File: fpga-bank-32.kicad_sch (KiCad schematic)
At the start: 1 part, among them U1 XC7K410T-2FFG900I

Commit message: Updated schematic page fields
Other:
- company: (none) -> Antmicro Ltd.
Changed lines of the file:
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@@
   (title_block
     (title "K410T devboard")
-    (date "2023-01-04")
+    (date "2023-01-27")
     (rev "0.0.99")
+    (company "Antmicro Ltd.")
   )
   (no_connect (at 143.51 124.46))

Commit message: Adding JTAG to FMC connector - in progress
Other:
- company: Antmicro Ltd. -> (none)
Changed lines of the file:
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@@
   (title_block
     (title "K410T devboard")
-    (date "2023-01-27")
+    (date "2023-01-04")
     (rev "0.0.99")
-    (company "Antmicro Ltd.")
   )
   (no_connect (at 143.51 124.46))

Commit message: Bump revision to 1.0.0. Update name on schematic and PCB sheets
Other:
- title: K410T devboard -> Kintex 410T devboard

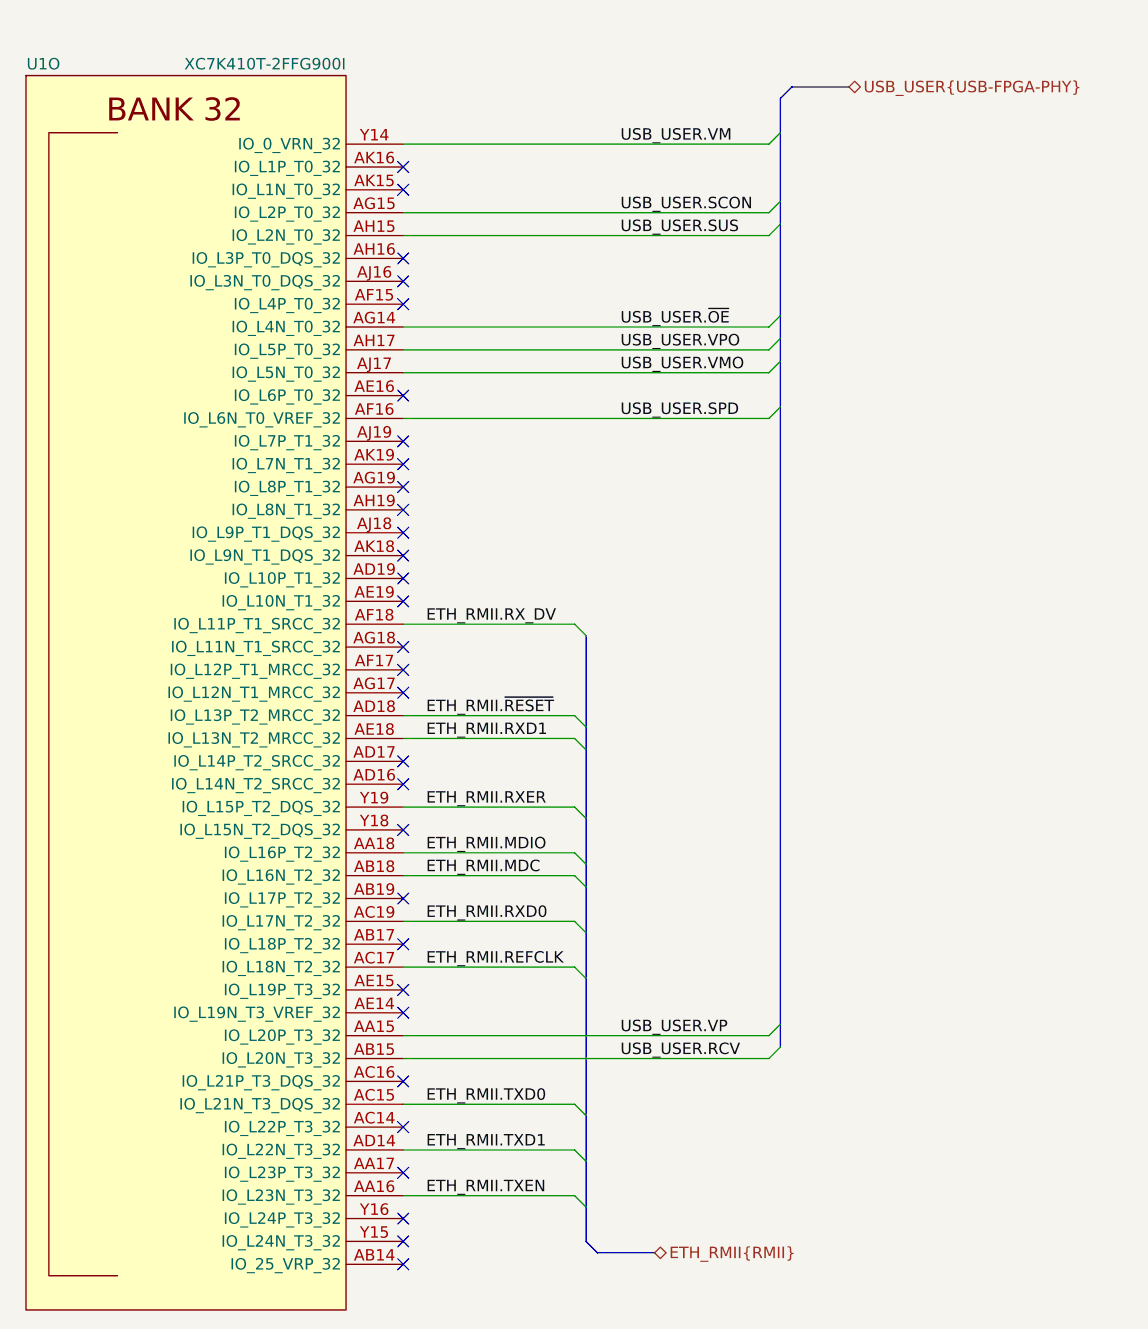
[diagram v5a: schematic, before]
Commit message: Introduce component standardization
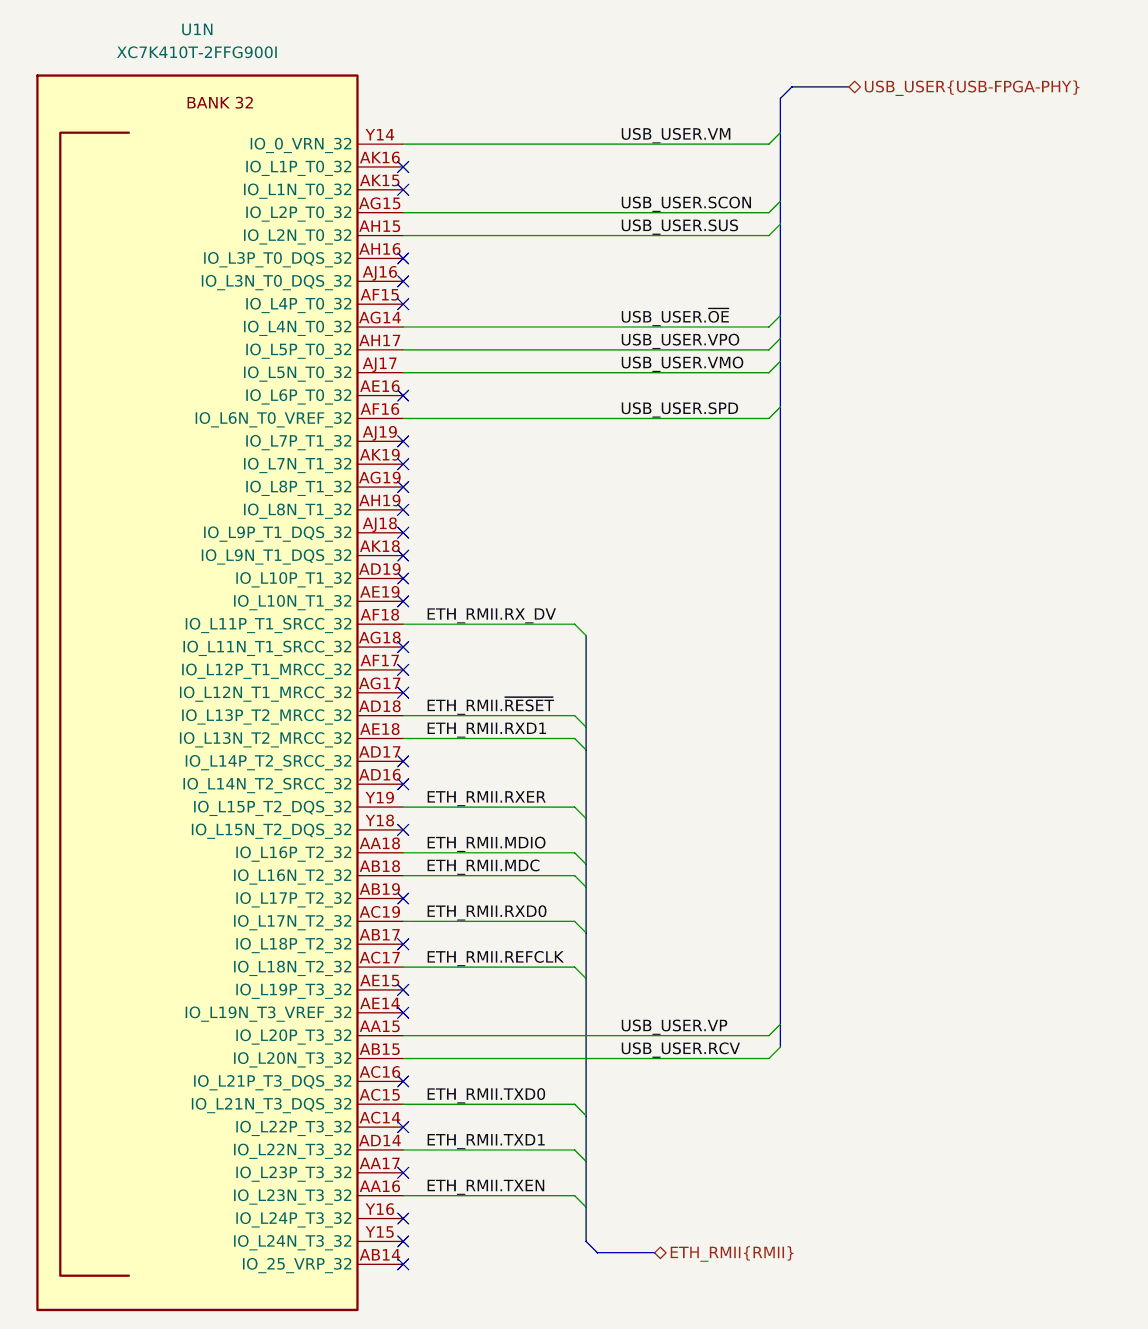
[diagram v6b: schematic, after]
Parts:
- removed U1: XC7K410T-2FFG900I, K410T-devboard-footprints:xc7k410t-2ffg900I, symbol K410T-devboard:XC7K410T-2FFG900I
- added U1: XC7K410T-2FFG900I, K410T-devboard-footprints:xc7k410t-2ffg900I, symbol K410T-devboard:XC7K410T-2FFG900I
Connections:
- net ETH_RMII.MDC: now also U1.AB18 (IO_L16N_T2_32)
- net ETH_RMII.MDIO: now also U1.AA18 (IO_L16P_T2_32)
- net ETH_RMII.REFCLK: now also U1.AC17 (IO_L18N_T2_32)
- net ETH_RMII.RXD0: now also U1.AC19 (IO_L17N_T2_32)
- net ETH_RMII.RXD1: now also U1.AE18 (IO_L13N_T2_MRCC_32)
- net ETH_RMII.RXER: now also U1.Y19 (IO_L15P_T2_DQS_32)
- net ETH_RMII.RX_DV: now also U1.AF18 (IO_L11P_T1_SRCC_32)
- net ETH_RMII.TXD0: now also U1.AC15 (IO_L21N_T3_DQS_32)
- net ETH_RMII.TXD1: now also U1.AD14 (IO_L22N_T3_32)
- net ETH_RMII.TXEN: now also U1.AA16 (IO_L23N_T3_32)
- net ETH_RMII.~{RESET}: now also U1.AD18 (IO_L13P_T2_MRCC_32)
- net USB_USER.RCV: now also U1.AB15 (IO_L20N_T3_32)
- net USB_USER.SCON: now also U1.AG15 (IO_L2P_T0_32)
- net USB_USER.SPD: now also U1.AF16 (IO_L6N_T0_VREF_32)
- net USB_USER.SUS: now also U1.AH15 (IO_L2N_T0_32)
- net USB_USER.VM: now also U1.Y14 (IO_0_VRN_32)
- net USB_USER.VMO: now also U1.AJ17 (IO_L5N_T0_32)
- net USB_USER.VP: now also U1.AA15 (IO_L20P_T3_32)
- net USB_USER.VPO: now also U1.AH17 (IO_L5P_T0_32)
- net USB_USER.~{OE}: now also U1.AG14 (IO_L4N_T0_32)
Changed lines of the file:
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@@
     (title "Kintex 410T devboard")
     (date "2023-02-01")
-    (rev "1.0.0")
+    (rev "1.1.1")
   )
   (no_connect (at 143.51 124.46))
@@
     (effects (font (size 1.27 1.27)) (justify left))
   )
-  (symbol (lib_id "K410T-devboard:XC7K410T-2FFG900I") (at 119.38 144.78 0) (unit 15)
-    (in_bom yes) (on_board yes)
-    (property "Reference" "U1" (id 0) (at 105.41 74.93 0)
-      (effects (font (size 1.27 1.27)) (justify right))
+  (symbol (lib_id "K410T-devboard:XC7K410T-2FFG900I") (at 143.51 83.82 0) (unit 14)
+    (in_bom yes) (on_board yes) (fields_autoplaced)
+    (property "Reference" "U1" (id 0) (at 120.65 71.12 0)
+      (effects (font (size 1.27 1.27) (thickness 0.15)))
     )
-    (property "Value" "XC7K410T-2FFG900I" (id 1) (at 137.16 74.93 0)
-      (effects (font (size 1.27 1.27)) (justify right))
+    (property "Value" "XC7K410T-2FFG900I" (id 1) (at 120.65 73.66 0)
+      (effects (font (size 1.27 1.27) (thickness 0.15)))
     )
-    (property "Footprint" "K410T-devboard-footprints:xc7k410t-2ffg900I" (id 2) (at 119.38 219.71 0)
-      (effects (font (size 1.27 1.27)) hide)
+    (property "Footprint" "K410T-devboard-footprints:xc7k410t-2ffg900I" (id 2) (at 143.51 57.15 0)
+      (effects (font (size 1.27 1.27) (thickness 0.15)) (justify left bottom) hide)
     )
-    (property "Datasheet" "https://eu.mouser.com/datasheet/2/903/ds180_7Series_Overview-1591537.pdf" (id 3) (at 119.38 222.25 0)
-      (effects (font (size 1.27 1.27)) hide)
+    (property "Datasheet" "https://eu.mouser.com/datasheet/2/903/ds180_7Series_Overview-1591537.pdf" (id 3) (at 143.51 59.69 0)
+      (effects (font (size 1.27 1.27) (thickness 0.15)) (justify left bottom) hide)
     )
-    (property "Manufacturer" "Xilinx" (id 4) (at 119.38 214.63 0)
-      (effects (font (size 1.27 1.27)) hide)
+    (property "Manufacturer" "Xilinx" (id 4) (at 143.51 62.23 0)
+      (effects (font (size 1.27 1.27) (thickness 0.15)) (justify left bottom) hide)
     )
-    (property "MPN" "XC7K410T-2FFG900I" (id 5) (at 119.38 217.17 0)
-      (effects (font (size 1.27 1.27)) hide)
+    (property "MPN" "XC7K410T-2FFG900I" (id 5) (at 143.51 64.77 0)
+      (effects (font (size 1.27 1.27) (thickness 0.15)) (justify left bottom) hide)
+    )
+    (property "Author" "Antmicro" (id 6) (at 143.51 67.31 0)
+      (effects (font (size 1.27 1.27) (thickness 0.15)) (justify left bottom) hide)
+    )
+    (property "License" "Apache-2.0" (id 7) (at 143.51 69.85 0)
+      (effects (font (size 1.27 1.27) (thickness 0.15)) (justify left bottom) hide)
     )
     (pin "AA20")
@@
     (pin "Y12")
     (pin "Y22")
-    (pin "C10")
-    (pin "M11")
-    (pin "M13")
-    (pin "M15")
-    (pin "M17")
-    (pin "N10")
-    (pin "N12")
-    (pin "N14")
-    (pin "N16")
-    (pin "N18")
-    (pin "P11")
-    (pin "P13")
-    (pin "P14")
-    (pin "P15")
-    (pin "P17")
-    (pin "R10")
-    (pin "R12")
-    (pin "R16")
-    (pin "R18")
-    (pin "T11")
-    (pin "T13")
-    (pin "T17")
-    (pin "U10")
-    (pin "U12")
-    (pin "U16")
-    (pin "U18")
-    (pin "V11")
-    (pin "V13")
-    (pin "V15")
-    (pin "V17")
-    (pin "W10")
-    (pin "W12")
-    (pin "W14")
-    (pin "W16")
-    (pin "W18")
     (pin "A1")
     (pin "A14")
@@
     (pin "B9")
     (pin "C1")
+    (pin "C10")
     (pin "C18")
     (pin "C2")
@@
     (pin "L6")
     (pin "L9")
+    (pin "M11")
     (pin "M12")
+    (pin "M13")
     (pin "M14")
+    (pin "M15")
     (pin "M16")
+    (pin "M17")
     (pin "M18")
     (pin "M21")
@@
     (pin "M9")
     (pin "N1")
+    (pin "N10")
     (pin "N11")
+    (pin "N12")
     (pin "N13")
+    (pin "N14")
     (pin "N15")
+    (pin "N16")
     (pin "N17")
+    (pin "N18")
     (pin "N2")
     (pin "N28")
@@
     (pin "N9")
     (pin "P10")
+    (pin "P11")
     (pin "P12")
+    (pin "P13")
+    (pin "P14")
+    (pin "P15")
     (pin "P16")
+    (pin "P17")
     (pin "P18")
     (pin "P25")
@@
     (pin "P9")
     (pin "R1")
+    (pin "R10")
     (pin "R11")
+    (pin "R12")
     (pin "R13")
+    (pin "R16")
     (pin "R17")
+    (pin "R18")
     (pin "R2")
     (pin "R22")
@@
     (pin "R9")
     (pin "T10")
+    (pin "T11")
     (pin "T12")
+    (pin "T13")
     (pin "T16")
+    (pin "T17")
     (pin "T18")
     (pin "T19")
@@
     (pin "T8")
     (pin "U1")
+    (pin "U10")
     (pin "U11")
+    (pin "U12")
     (pin "U13")
+    (pin "U16")
     (pin "U17")
+    (pin "U18")
     (pin "U2")
     (pin "U26")
@@
     (pin "U9")
     (pin "V10")
+    (pin "V11")
     (pin "V12")
+    (pin "V13")
     (pin "V14")
+    (pin "V15")
     (pin "V16")
+    (pin "V17")
     (pin "V18")
     (pin "V23")
@@
     (pin "V9")
     (pin "W1")
+    (pin "W10")
     (pin "W11")
+    (pin "W12")
     (pin "W13")
+    (pin "W14")
     (pin "W15")
+    (pin "W16")
     (pin "W17")
+    (pin "W18")
     (pin "W2")
     (pin "W20")
